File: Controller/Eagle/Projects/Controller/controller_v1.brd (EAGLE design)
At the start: 100 x 80 mm, 47 parts, among them J1 BATT, U1 V_REG_317SMD, U2 ATMEGA128RFA1, U3 RF_AMPLIFIER, Y1 32.768kHz, Y2 16MHz

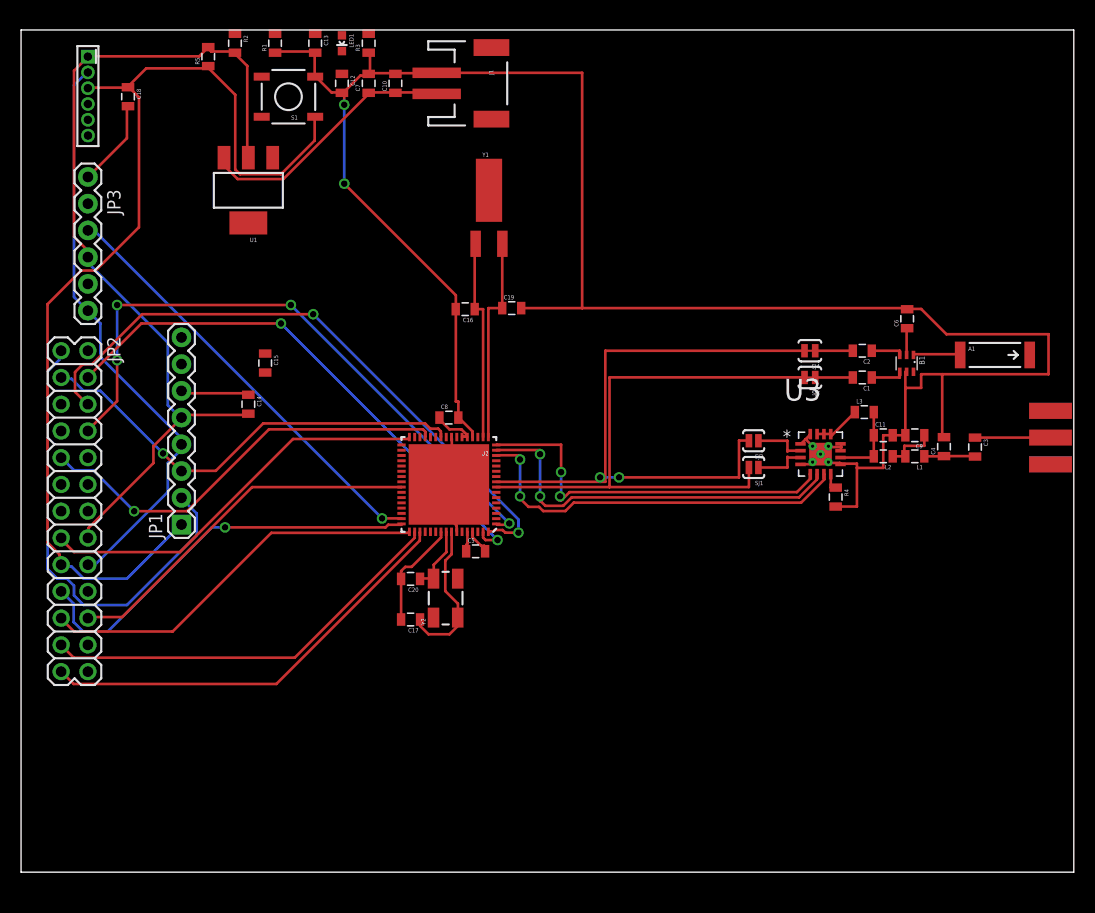
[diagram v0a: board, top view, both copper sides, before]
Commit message: Finished first version of of the controller board, all of the way to routing Stil need to pass checks for the schematic, but i will ask about those in class today.
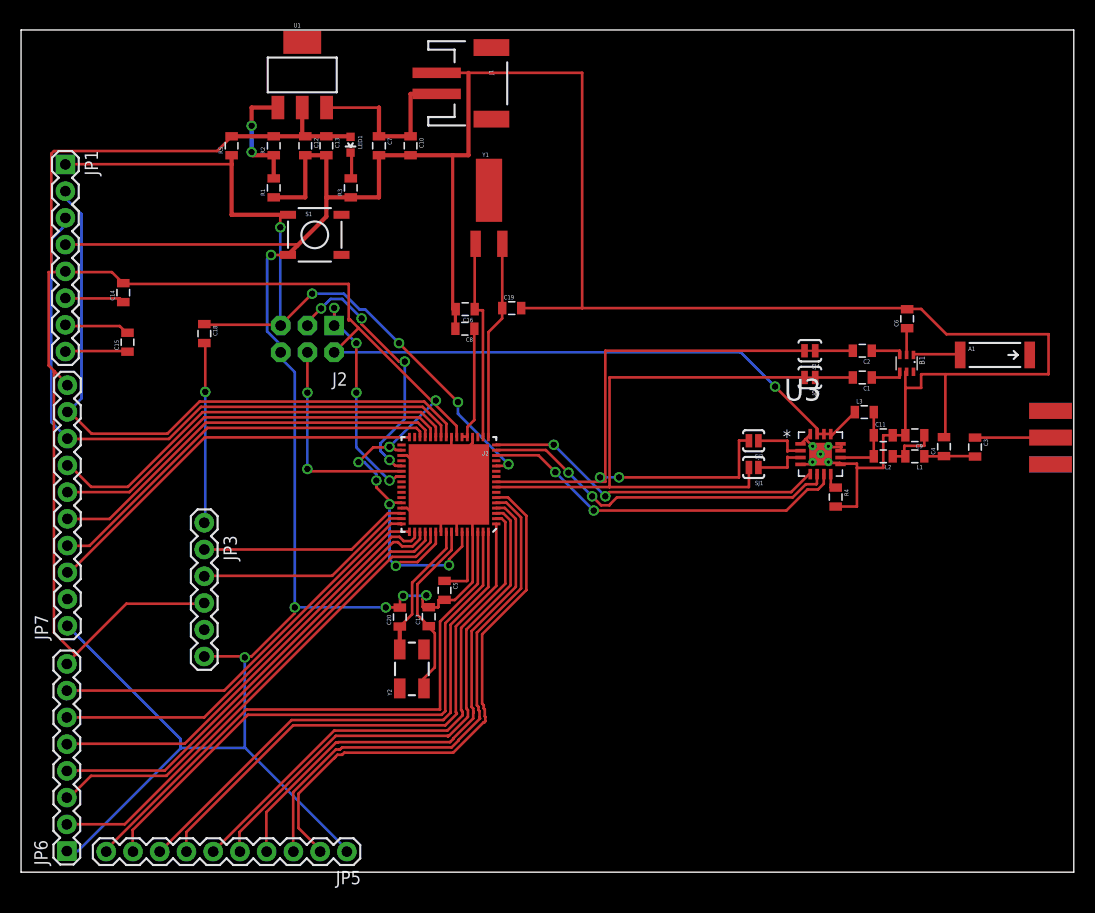
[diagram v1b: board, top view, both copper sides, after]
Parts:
- removed JP2: M13X22X13, SparkFun-Connectors:2X13
- removed JP4: AVR_MINI_PROGSMD, Controller:AVR_MINI_PROG
- added J2: AVR_SPI_PRG_6NS, Controller:2X3-NS
- added JP5, JP7: M10", Controller:1X10
- added JP6: (no value), Controller:1X08
- moved JP1 35.9 mm to (4.21, 67.2), turned to 270 degrees
- moved JP3 34.7 mm to (17.4, 33.2)
- moved C18 23.6 mm to (17.4, 51.2)
- moved C14 15.9 mm to (9.71, 55.0), turned to 90 degrees
- moved R3 13.8 mm to (31.3, 65.0)
- moved R1 13.7 mm to (24.0, 65.0)
- moved S1 13.4 mm to (27.9, 60.5), turned to 0 degrees
- moved C15 13.2 mm to (10.1, 50.3), turned to 90 degrees
- moved U1 12.1 mm to (26.7, 75.7), turned to 0 degrees
- moved R2 10.4 mm to (24.0, 69.0), turned to 90 degrees
- moved C13 9.80 mm to (29.0, 69.0)
- moved LED1 9.67 mm to (31.3, 69.1)
- moved R5 8.76 mm to (20.0, 69.0)
- moved C8 8.58 mm to (42.2, 51.6), turned to 180 degrees
- moved Y2 7.45 mm to (37.1, 19.3)
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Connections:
- new net PD8: JP7.2
- new net PE6: JP6.3, U2.52
- new net PE7: JP6.2, U2.53
- net 3.3V: now also J2.2, JP6.8, JP7.10; no longer JP2.16, JP4.1
- net ADC0: now also JP5.9; no longer JP2.4
- net ADC1: now also JP5.8; no longer JP2.6
- net ADC2: now also JP5.7; no longer JP2.8
- net ADC3: now also JP5.6
- net ADC4: now also JP5.5
- net ADC5: now also JP5.4; no longer JP2.10
- net ADC6: now also JP5.3; no longer JP2.12
- net ADC7: now also JP5.2; no longer JP2.14
- net AREF: now also JP5.10; no longer JP2.2
- net GND: now also J2.6, JP5.1, JP6.1, JP7.1; no longer JP2.18, JP4.2
- net MISO: now also J2.1; no longer JP4.6
- net MOSI: now also J2.4; no longer JP4.4
- net PB4: no longer JP2.20
- net PB5: no longer JP2.22
- net PB6: no longer JP2.24
- net PB7: no longer JP2.26
- net PD0/I2C_SCL: now also JP7.9; no longer JP2.1
- net PD1/I2C_SDA: now also JP7.8; no longer JP2.3
- net PD2/RXD1: now also JP7.7; no longer JP2.5
- net PD3/TXD1: now also JP7.6; no longer JP2.7
- net PD4: now also JP7.5; no longer JP2.9
- net PD5: now also JP7.4; no longer JP2.11
- net PD6: no longer JP2.13
- net PD7: now also JP7.3; no longer JP2.15
- net PE2: now also JP6.7; no longer JP2.19
- net PE3: now also JP6.6; no longer JP2.21
- net PE4: now also JP6.5; no longer JP2.23
- net PE5: now also JP6.4; no longer JP2.25
- net RESET_N: now also J2.5; no longer JP2.17, JP4.3
- net SCK: now also J2.3; no longer JP4.5
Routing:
- net 3.3V: track 90.5 -> 242.3 mm, vias 0 -> 8
- net GND: track 284.5 -> 398.8 mm, vias 2 -> 6
- net AREF: track 0.00 -> 55.8 mm
- net ADC7: track 0.00 -> 52.0 mm
- net ADC4: track 0.00 -> 50.3 mm
- net ADC6: track 0.00 -> 50.2 mm
- net ADC5: track 0.00 -> 50.2 mm
- net ADC3: track 0.00 -> 50.2 mm
- net PE7: track 0.00 -> 46.6 mm
- net PE6: track 0.00 -> 45.0 mm
- net PD2/RXD1: track 0.00 -> 40.4 mm
- net PD5: track 0.00 -> 38.8 mm
- net PD3/TXD1: track 0.00 -> 38.7 mm
- net PB5: track 35.0 -> 0.00 mm
- net SCK: track 0.00 -> 25.3 mm, vias 0 -> 4
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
